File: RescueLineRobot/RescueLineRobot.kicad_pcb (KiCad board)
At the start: 2 copper layers, 80 x 110 mm, 18 parts

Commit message: Fix GerberV2
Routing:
- net D21: track 108.5 -> 90.1 mm
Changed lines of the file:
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@@
 	)
 	(segment
-		(start 123.725 85.3)
-		(end 123.725 72)
-		(width 0.4)
-		(layer "B.Cu")
-		(net 5)
-	)
-	(segment
-		(start 123.725 85.3)
-		(end 126.225 82.8)
-		(width 0.4)
-		(layer "B.Cu")
-		(net 5)
-	)
-	(segment
-		(start 123.5 93.25)
-		(end 127.75 97.5)
+		(start 122.55 84.2)
+		(end 123.5 83.25)
 		(width 0.4)
 		(layer "B.Cu")
@@
 	)
 	(segment
-		(start 122.725 73)
-		(end 122.55 73.175)
-		(width 0.4)
-		(layer "B.Cu")
-		(net 5)
-	)
-	(segment
-		(start 122.725 73)
-		(end 123.725 72)
+		(start 123.5 80.25)
+		(end 123.5 72.25)
+		(width 0.4)
+		(layer "B.Cu")
+		(net 5)
+	)
+	(segment
+		(start 123.5 72.25)
+		(end 123.4875 72.2375)
 		(width 0.4)
 		(layer "B.Cu")
@@
 	)
 	(segment
-		(start 123.5 78.25)
+		(start 123.5 83.25)
 		(end 123.5 93.25)
-		(width 0.4)
-		(layer "B.Cu")
-		(net 5)
-	)
-	(segment
-		(start 127.75 97.5)
-		(end 128.5 97.5)
-		(width 0.4)
-		(layer "B.Cu")
-		(net 5)
-	)
-	(segment
-		(start 122.55 73.175)
-		(end 122.55 84.2)
 		(width 0.4)
 		(layer "B.Cu")
@@
 	)
 	(segment
+		(start 128.5 82.8)
+		(end 126.05 82.8)
+		(width 0.4)
+		(layer "B.Cu")
+		(net 5)
+	)
+	(segment
+		(start 126.05 82.8)
+		(end 123.5 80.25)
+		(width 0.4)
+		(layer "B.Cu")
+		(net 5)
+	)
+	(segment
 		(start 125.225 70.5)
 		(end 123.725 72)
@@
 	)
 	(segment
+		(start 128.5 97.5)
+		(end 126.75 97.5)
+		(width 0.4)
+		(layer "B.Cu")
+		(net 5)
+	)
+	(segment
 		(start 127 70.5)
 		(end 125.225 70.5)
@@
 	)
 	(segment
-		(start 126.225 82.8)
-		(end 128.5 82.8)
+		(start 123.5 80.25)
+		(end 123.5 83.25)
+		(width 0.4)
+		(layer "B.Cu")
+		(net 5)
+	)
+	(segment
+		(start 123.4875 72.2375)
+		(end 123.725 72)
+		(width 0.4)
+		(layer "B.Cu")
+		(net 5)
+	)
+	(segment
+		(start 126.75 97.5)
+		(end 123.5 94.25)
+		(width 0.4)
+		(layer "B.Cu")
+		(net 5)
+	)
+	(segment
+		(start 123.5 94.25)
+		(end 123.5 109)
 		(width 0.4)
 		(layer "B.Cu")
@@
 	(segment
 		(start 123.5 93.25)
-		(end 123.5 109)
+		(end 123.5 94.25)
 		(width 0.4)
 		(layer "B.Cu")
@@
 	(segment
 		(start 125.2 79.275)
+		(end 125.2 93.75)
+		(width 0.4)
+		(layer "F.Cu")
+		(net 27)
+	)
+	(segment
+		(start 125.2 93.75)
 		(end 125.2 96.3)
-		(width 0.4)
-		(layer "F.Cu")
-		(net 27)
-	)
-	(segment
-		(start 125.2 96.3)
-		(end 126.5 95)
 		(width 0.4)
 		(layer "F.Cu")
@@
 	(segment
 		(start 126.5 95)
+		(end 125.25 93.75)
+		(width 0.4)
+		(layer "F.Cu")
+		(net 27)
+	)
+	(segment
+		(start 126.5 95)
 		(end 128.5 95)
 		(width 0.4)
@@
 		(width 0.4)
 		(layer "F.Cu")
+		(net 27)
+	)
+	(segment
+		(start 125.25 93.75)
+		(end 125.2 93.75)
+		(width 0.4)
+		(layer "F.Cu")

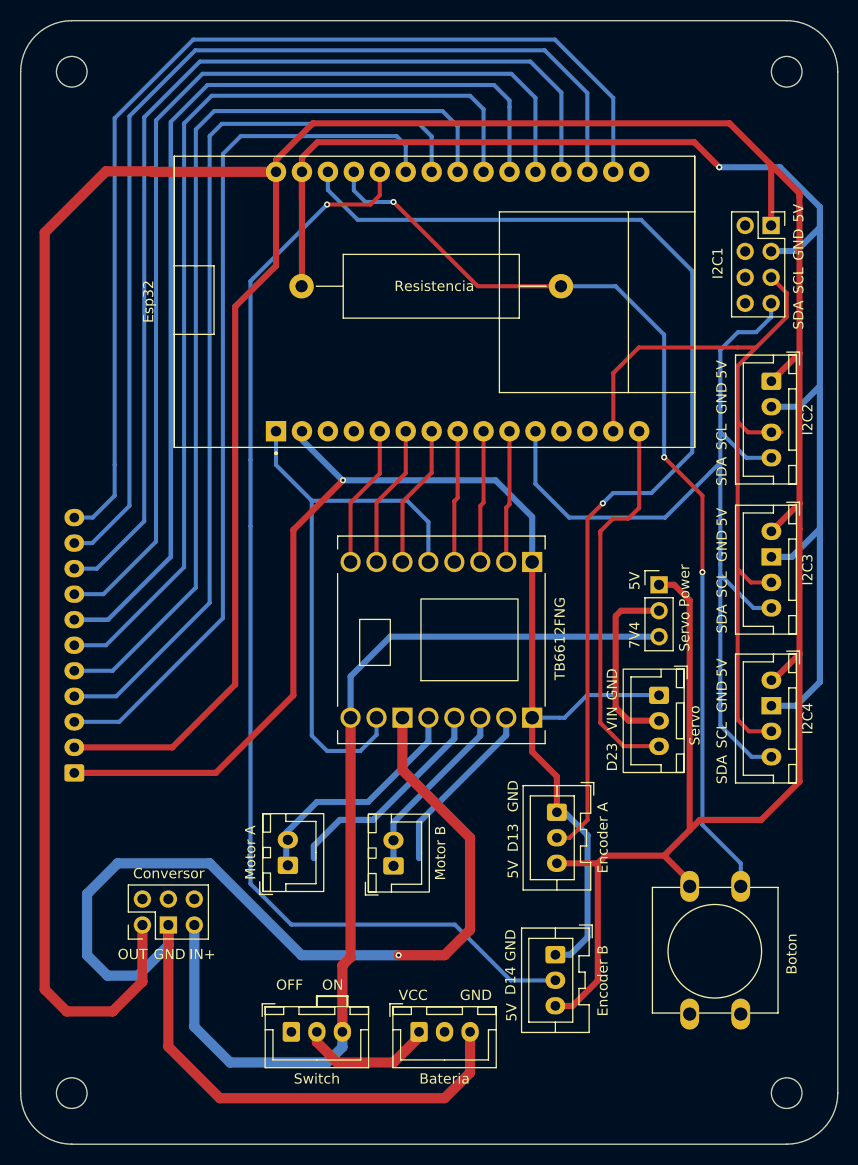
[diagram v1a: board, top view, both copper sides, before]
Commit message: Last pcb changes
Arreglo de puerto i2c para el giroscopio
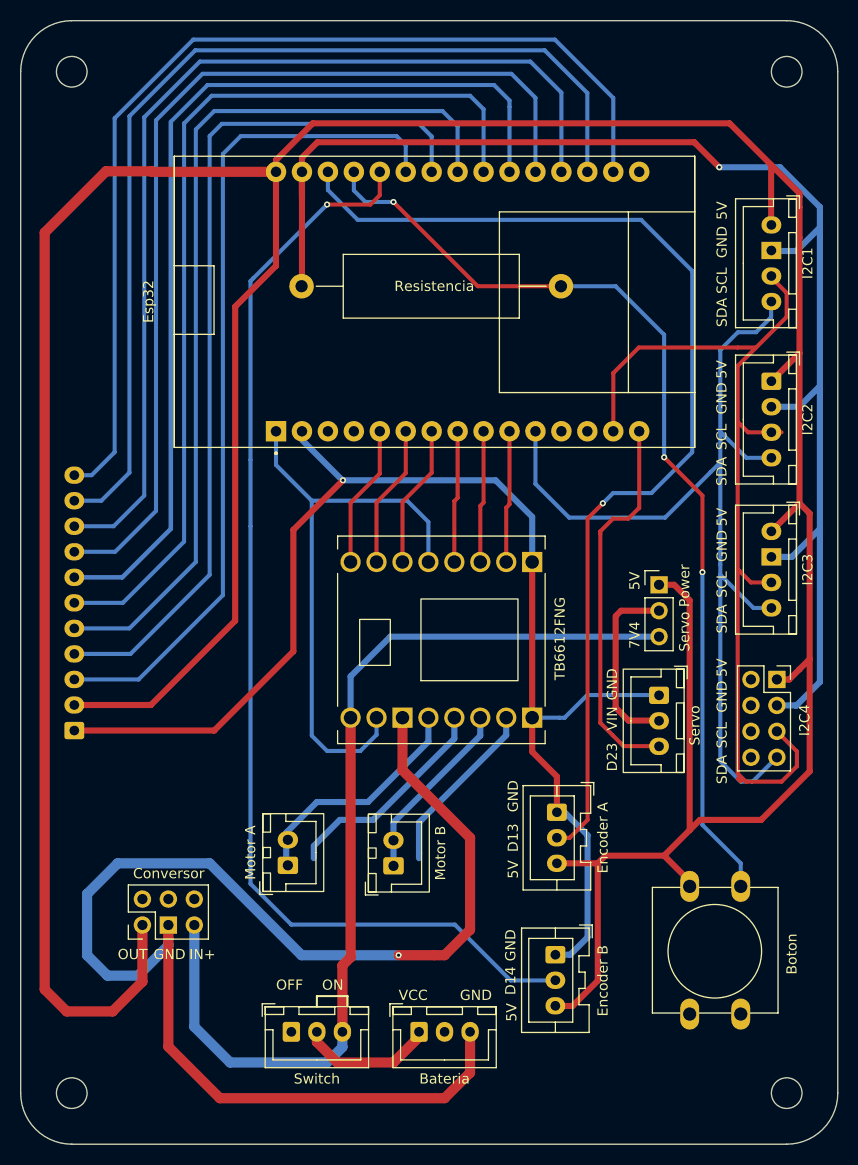
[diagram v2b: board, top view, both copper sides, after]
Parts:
- moved I2C1 44.6 mm to (128.5, 60.0)
- moved I2C4 44.5 mm to (129.0, 104.5)
- moved SigueLineas1 4.15 mm to (60.2, 109.5)
- renumbered I2C4 to I2C1, I2C1 to I2C4
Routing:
- net D22: track 79.0 -> 91.9 mm
- net GND: track 409.7 -> 405.0 mm
- net D21: track 90.1 -> 94.7 mm
- net 5V: track 392.3 -> 388.0 mm
- net D36: track 103.4 -> 99.2 mm
- net D39: track 102.0 -> 98.4 mm
- net D35: track 98.6 -> 95.2 mm
- net D26: track 89.0 -> 85.6 mm
- net D32: track 96.9 -> 93.6 mm
- net D34: track 100.4 -> 97.3 mm
- net D33: track 94.5 -> 91.3 mm
- net D25: track 91.6 -> 88.4 mm
- net D27: track 85.8 -> 82.8 mm
